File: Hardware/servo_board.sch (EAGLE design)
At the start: 33 parts, among them U1 PCA9685, U2 PCA9306

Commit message: Add version info
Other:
- note added: "01"
- note added: "M Hord"
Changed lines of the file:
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@@
 <sheet>
 <plain>
+<text x="165.1" y="7.62" size="3.81" layer="91">M Hord</text>
+<text x="237.744" y="6.35" size="3.81" layer="91">01</text>
 </plain>
 <instances>

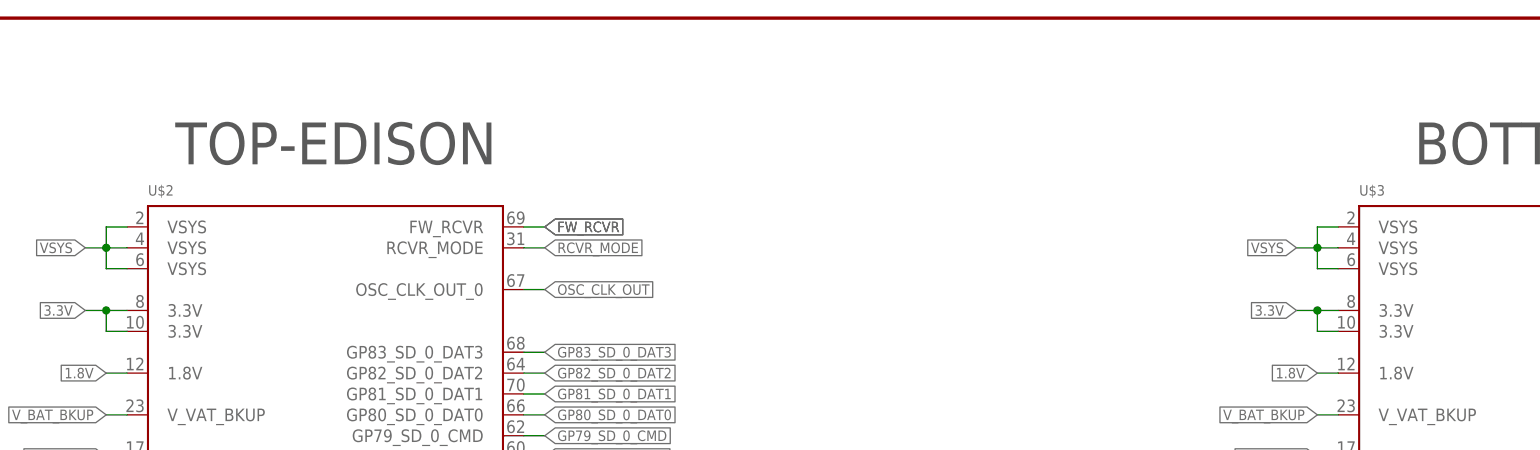
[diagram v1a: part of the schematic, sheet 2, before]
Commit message: Touch up silk, resistor placement
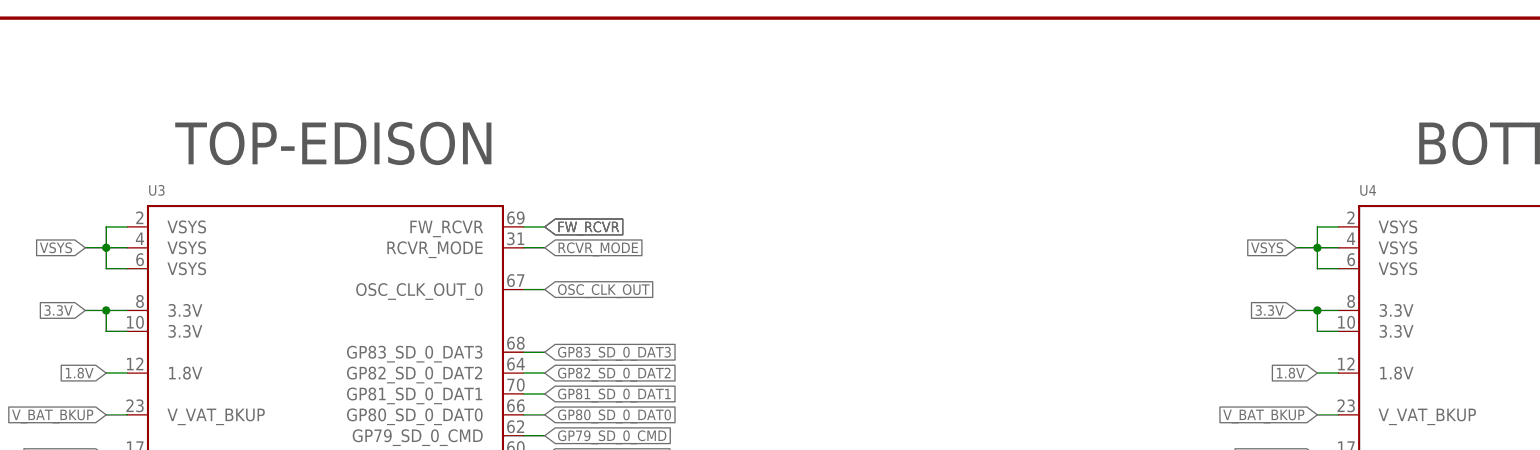
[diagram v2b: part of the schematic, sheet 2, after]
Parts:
- renumbered U$2 to U3, U$3 to U4

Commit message: Incorporate review changes
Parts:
- added FID1, FID2: FIDUCIALUFIDUCIAL, SparkFun-Aesthetics:FIDUCIALUFIDUCIAL
- added LOGO1: SFE_LOGO_NAME_FLAME.1_INCH, SparkFun-Aesthetics:SFE_LOGO_NAME_FLAME.1_INCH
- added LOGO4: OSHW-LOGOS, SparkFun-Aesthetics:OSHW-LOGOS
- added R14, R15, R16, R17, R18, R19: 1K, SparkFun-Resistors:1KOHM1/10W1%(0603)
- added SJ1, SJ2, SJ3, SJ4, SJ5, SJ6: JUMPER-PAD-2-NOYES_SILK, SparkFun-Passives:JUMPER-PAD-2-NOYES_SILK
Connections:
- new net A0: R14.2, SJ1.2, U1.A0
- new net A1: R15.2, SJ2.2, U1.A1
- new net A2: R16.2, SJ3.2, U1.A2
- new net A3: R17.2, SJ4.2, U1.A3
- new net A4: R18.2, SJ5.2, U1.A4
- new net A5: R19.2, SJ6.2, U1.A5
- net GND: now also R14.1, R15.1, R16.1, R17.1, R18.1, R19.1; no longer U1.A3, U1.A4, U1.A5
- net VSYS: now also SJ1.1, SJ2.1, SJ3.1, SJ4.1, SJ5.1, SJ6.1
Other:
- note added: "A0"
- note added: "A1"
- note added: "A2"
- note added: "A3"
- note added: "A4"
- note added: "A5"
- note added: "I2C Address is 0b1xxxxxx. Default is 0b1000000; to set a bit, close that bit's jumper."
- moved on the sheet: C1, C2, C3, R1, R10, R11, R12, R13, R2, R3, R4, R5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

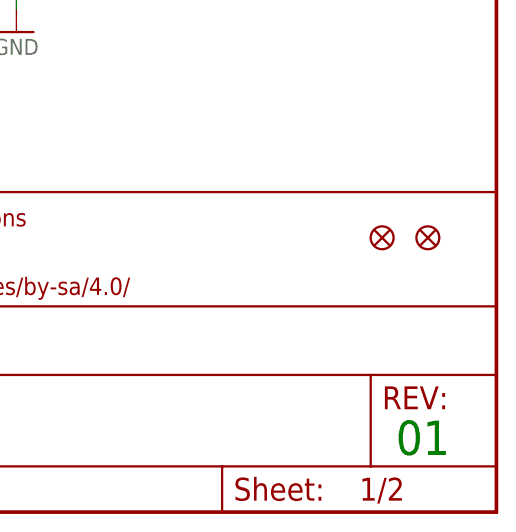
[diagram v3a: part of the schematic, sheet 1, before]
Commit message: Fix fids, remove weird name
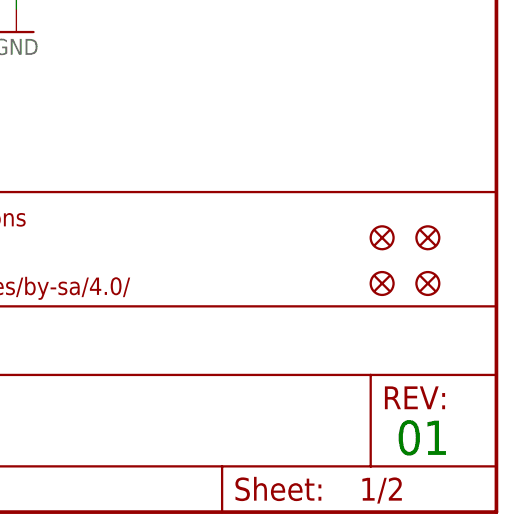
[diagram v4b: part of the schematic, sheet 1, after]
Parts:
- added FID3, FID4: FIDUCIAL1X2, SparkFun-Aesthetics:FIDUCIAL1X2
- FID1, FID2: value FIDUCIALUFIDUCIAL -> FIDUCIAL1X2; device SparkFun-Aesthetics:FIDUCIALUFIDUCIAL -> SparkFun-Aesthetics:FIDUCIAL1X2
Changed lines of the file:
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@@
 <part name="LOGO1" library="SparkFun-Aesthetics" deviceset="SFE_LOGO_NAME_FLAME" device=".1_INCH"/>
 <part name="LOGO4" library="SparkFun-Aesthetics" deviceset="OSHW-LOGO" device="S"/>
-<part name="FID1" library="SparkFun-Aesthetics" deviceset="FIDUCIAL" device="UFIDUCIAL"/>
-<part name="FID2" library="SparkFun-Aesthetics" deviceset="FIDUCIAL" device="UFIDUCIAL"/>
+<part name="FID1" library="SparkFun-Aesthetics" deviceset="FIDUCIAL" device="1X2" value="FIDUCIAL1X2"/>
+<part name="FID2" library="SparkFun-Aesthetics" deviceset="FIDUCIAL" device="1X2" value="FIDUCIAL1X2"/>
 <part name="R14" library="SparkFun-Resistors" deviceset="1KOHM1/10W1%(0603)" device="" value="1K"/>
 <part name="R15" library="SparkFun-Resistors" deviceset="1KOHM1/10W1%(0603)" device="" value="1K"/>
@@
 <part name="SJ6" library="SparkFun-Passives" deviceset="JUMPER-PAD-2-NO" device="YES_SILK"/>
 <part name="GND9" library="SparkFun-Aesthetics" deviceset="GND" device=""/>
+<part name="FID3" library="SparkFun-Aesthetics" deviceset="FIDUCIAL" device="1X2" value="FIDUCIAL1X2"/>
+<part name="FID4" library="SparkFun-Aesthetics" deviceset="FIDUCIAL" device="1X2" value="FIDUCIAL1X2"/>
 </parts>
 <sheets>
@@
 </instance>
 <instance part="GND9" gate="1" x="157.48" y="48.26"/>
+<instance part="FID3" gate="G$1" x="236.22" y="25.4"/>
+<instance part="FID4" gate="G$1" x="241.3" y="25.4"/>
 </instances>
 <busses>
